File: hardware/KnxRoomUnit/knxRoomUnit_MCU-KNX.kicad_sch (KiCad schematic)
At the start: 26 parts, among them J1 KNX, J2 PROG, Q1 S8050, Q2 S8050, SW1 rst, SW2 UI_UP, SW3 KNX_PROG, SW4 UI_DW, SW5 UI_OK, U2 ESP32-WROOM-32

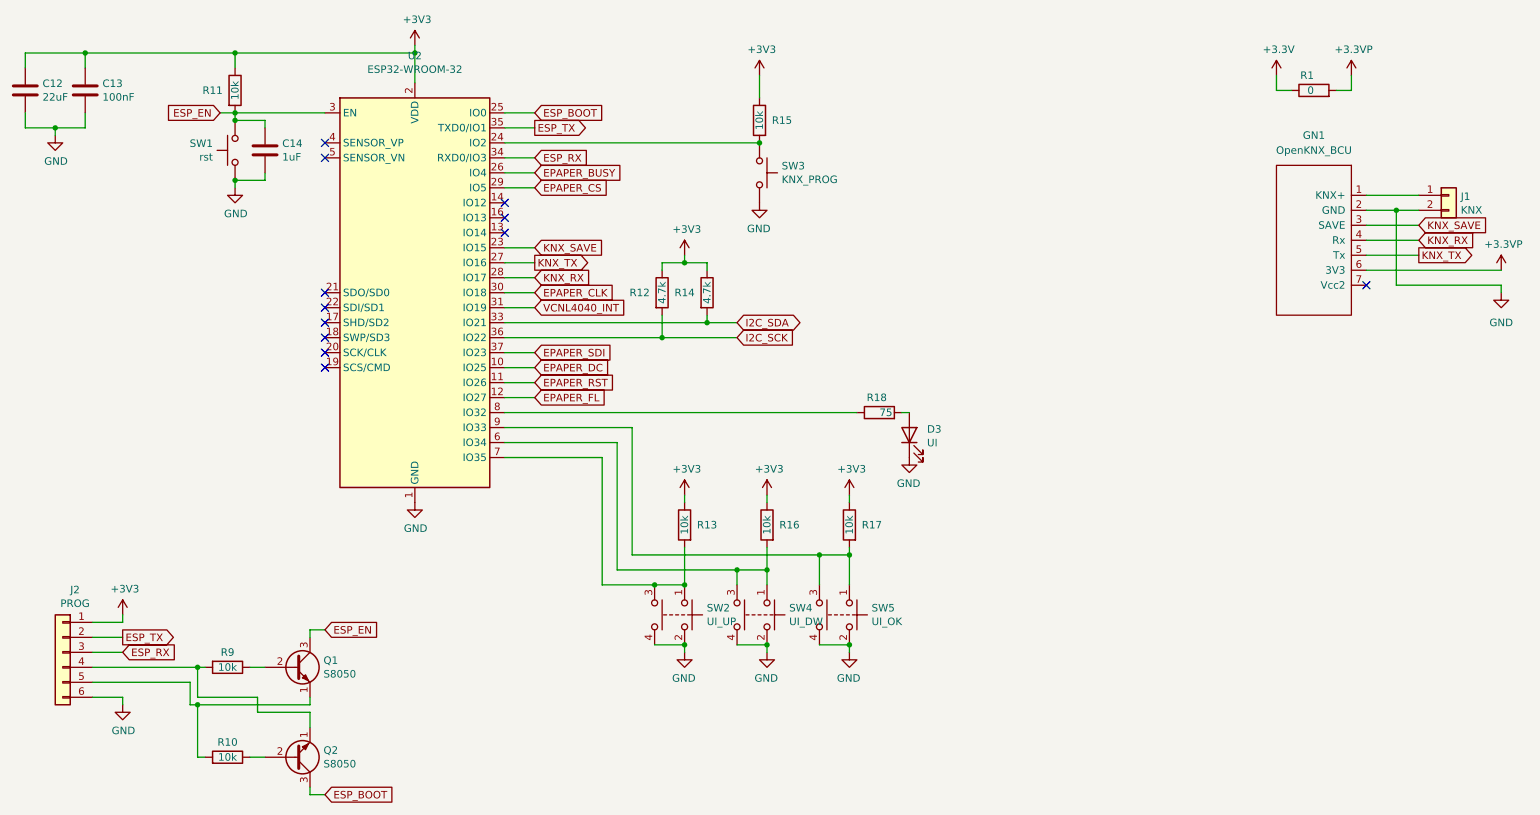
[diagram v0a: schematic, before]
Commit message: Updated sensors
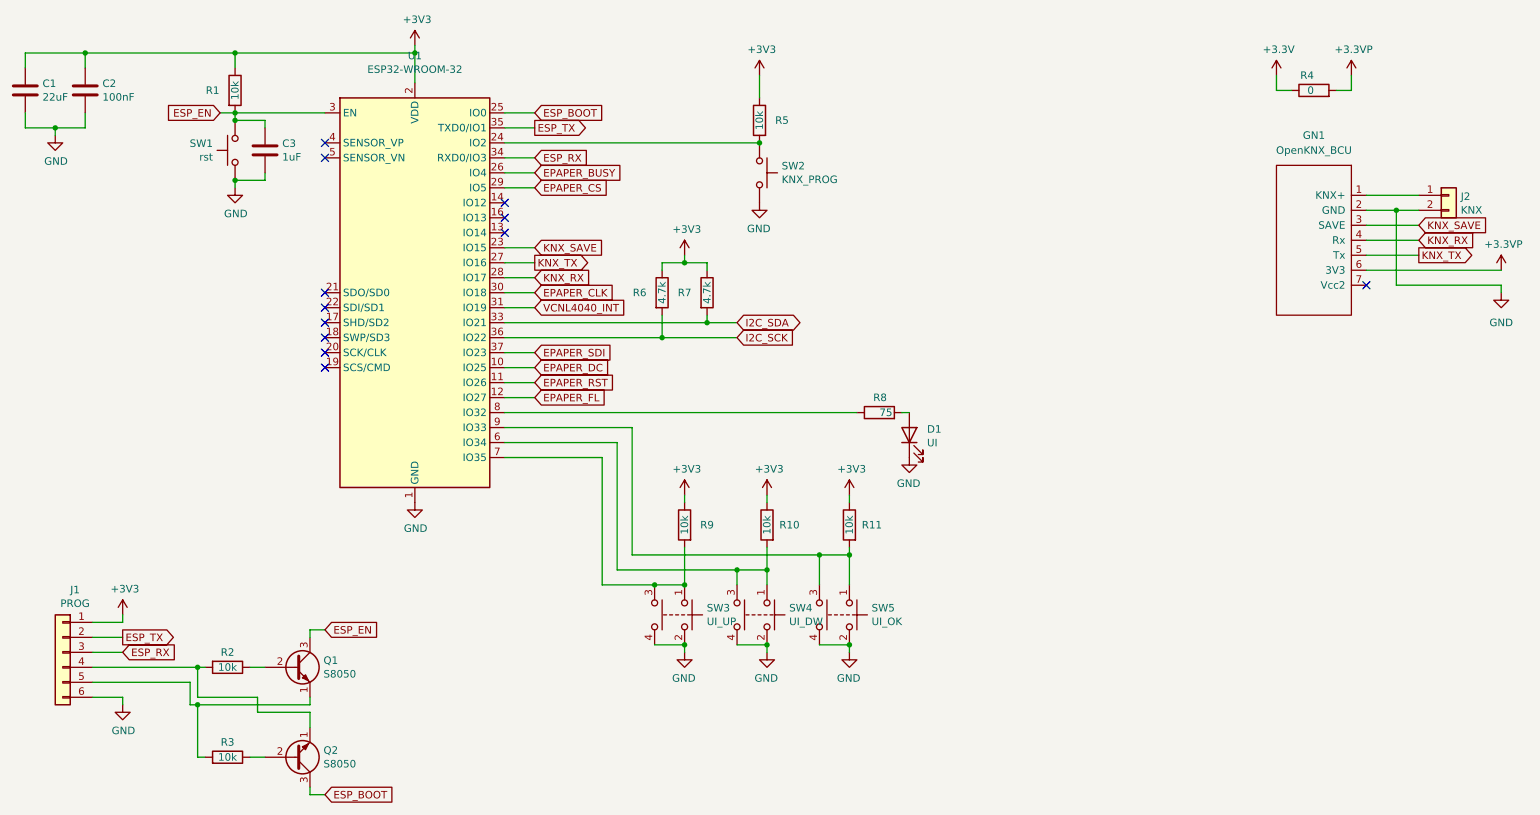
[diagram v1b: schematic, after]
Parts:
- renumbered C12 to C1, C13 to C2, C14 to C3, D3 to D1, J2 to J1, J1 to J2, R11 to R1, R16 to R10, R17 to R11, R9 to R2, R10 to R3, R1 to R4, R15 to R5, R12 to R6, R14 to R7, R18 to R8, R13 to R9, SW3 to SW2, SW2 to SW3, U2 to U1
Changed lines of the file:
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@@
   (symbol (lib_id "Switch:SW_Push_Dual") (at 130.81 118.11 270) (unit 1)
     (in_bom yes) (on_board yes) (dnp no)
-    (property "Reference" "SW2" (at 134.5692 116.9416 90)
+    (property "Reference" "SW3" (at 134.5692 116.9416 90)
       (effects (font (size 1.27 1.27)) (justify left))
     )
@@
       (project "knxRoomUnit"
         (path "/699feae1-8cdd-4d2b-947f-f24849c73cdb/00000000-0000-0000-0000-00006045b179"
-          (reference "SW2") (unit 1)
+          (reference "SW3") (unit 1)
         )
       )
@@
   (symbol (lib_id "Device:R") (at 130.81 102.87 0) (mirror y) (unit 1)
     (in_bom yes) (on_board yes) (dnp no)
-    (property "Reference" "R13" (at 134.62 102.87 0)
+    (property "Reference" "R9" (at 134.62 102.87 0)
       (effects (font (size 1.27 1.27)))
     )
@@
       (project "knxRoomUnit"
         (path "/699feae1-8cdd-4d2b-947f-f24849c73cdb/00000000-0000-0000-0000-00006045b179"
-          (reference "R13") (unit 1)
+          (reference "R9") (unit 1)
         )
       )
@@
   (symbol (lib_id "Device:R") (at 144.78 102.87 0) (mirror y) (unit 1)
     (in_bom yes) (on_board yes) (dnp no)
-    (property "Reference" "R16" (at 148.59 102.87 0)
+    (property "Reference" "R10" (at 148.59 102.87 0)
       (effects (font (size 1.27 1.27)))
     )
@@
       (project "knxRoomUnit"
         (path "/699feae1-8cdd-4d2b-947f-f24849c73cdb/00000000-0000-0000-0000-00006045b179"
-          (reference "R16") (unit 1)
+          (reference "R10") (unit 1)
         )
       )
@@
   (symbol (lib_id "Device:R") (at 158.75 102.87 0) (mirror y) (unit 1)
     (in_bom yes) (on_board yes) (dnp no)
-    (property "Reference" "R17" (at 162.56 102.87 0)
+    (property "Reference" "R11" (at 162.56 102.87 0)
       (effects (font (size 1.27 1.27)))
     )
@@
       (project "knxRoomUnit"
         (path "/699feae1-8cdd-4d2b-947f-f24849c73cdb/00000000-0000-0000-0000-00006045b179"
-          (reference "R17") (unit 1)
+          (reference "R11") (unit 1)
         )
       )
@@
   (symbol (lib_id "Device:C") (at 19.05 29.21 0) (unit 1)
     (in_bom yes) (on_board yes) (dnp no)
-    (property "Reference" "C12" (at 21.971 28.0416 0)
+    (property "Reference" "C1" (at 21.971 28.0416 0)
       (effects (font (size 1.27 1.27)) (justify left))
     )
@@
       (project "knxRoomUnit"
         (path "/699feae1-8cdd-4d2b-947f-f24849c73cdb/00000000-0000-0000-0000-00006045b179"
-          (reference "C12") (unit 1)
+          (reference "C1") (unit 1)
         )
       )
@@
   (symbol (lib_id "Device:C") (at 29.21 29.21 0) (unit 1)
     (in_bom yes) (on_board yes) (dnp no)
-    (property "Reference" "C13" (at 32.131 28.0416 0)
+    (property "Reference" "C2" (at 32.131 28.0416 0)
       (effects (font (size 1.27 1.27)) (justify left))
     )
@@
       (project "knxRoomUnit"
         (path "/699feae1-8cdd-4d2b-947f-f24849c73cdb/00000000-0000-0000-0000-00006045b179"
-          (reference "C13") (unit 1)
+          (reference "C2") (unit 1)
         )
       )
@@
   (symbol (lib_id "Device:R") (at 53.34 127 270) (unit 1)
     (in_bom yes) (on_board yes) (dnp no)
-    (property "Reference" "R9" (at 53.34 124.46 90)
+    (property "Reference" "R2" (at 53.34 124.46 90)
       (effects (font (size 1.27 1.27)))
     )
@@
       (project "knxRoomUnit"
         (path "/699feae1-8cdd-4d2b-947f-f24849c73cdb/00000000-0000-0000-0000-00006045b179"
-          (reference "R9") (unit 1)
+          (reference "R2") (unit 1)
         )
       )
@@
   (symbol (lib_id "Device:R") (at 53.34 142.24 270) (mirror x) (unit 1)
     (in_bom yes) (on_board yes) (dnp no)
-    (property "Reference" "R10" (at 53.34 139.7 90)
+    (property "Reference" "R3" (at 53.34 139.7 90)
       (effects (font (size 1.27 1.27)))
     )
@@
       (project "knxRoomUnit"
         (path "/699feae1-8cdd-4d2b-947f-f24849c73cdb/00000000-0000-0000-0000-00006045b179"
-          (reference "R10") (unit 1)
+          (reference "R3") (unit 1)
         )
       )
@@
   (symbol (lib_id "Connector_Generic:Conn_01x06") (at 25.4 124.46 0) (mirror y) (unit 1)
     (in_bom yes) (on_board yes) (dnp no)
-    (property "Reference" "J2" (at 27.4828 113.8682 0)
+    (property "Reference" "J1" (at 27.4828 113.8682 0)
       (effects (font (size 1.27 1.27)))
     )
@@
       (project "knxRoomUnit"
         (path "/699feae1-8cdd-4d2b-947f-f24849c73cdb/00000000-0000-0000-0000-00006045b179"
-          (reference "J2") (unit 1)
+          (reference "J1") (unit 1)
         )
       )
@@
   (symbol (lib_id "Switch:SW_Push") (at 143.51 43.18 270) (unit 1)
     (in_bom yes) (on_board yes) (dnp no)
-    (property "Reference" "SW3" (at 147.2692 42.0116 90)
+    (property "Reference" "SW2" (at 147.2692 42.0116 90)
       (effects (font (size 1.27 1.27)) (justify left))
     )
@@
       (project "knxRoomUnit"
         (path "/699feae1-8cdd-4d2b-947f-f24849c73cdb/00000000-0000-0000-0000-00006045b179"
-          (reference "SW3") (unit 1)
+          (reference "SW2") (unit 1)
         )
       )
@@
   (symbol (lib_id "Device:R") (at 143.51 34.29 0) (mirror y) (unit 1)
     (in_bom yes) (on_board yes) (dnp no)
-    (property "Reference" "R15" (at 147.32 34.29 0)
+    (property "Reference" "R5" (at 147.32 34.29 0)
       (effects (font (size 1.27 1.27)))
     )
@@
       (project "knxRoomUnit"
         (path "/699feae1-8cdd-4d2b-947f-f24849c73cdb/00000000-0000-0000-0000-00006045b179"
-          (reference "R15") (unit 1)
+          (reference "R5") (unit 1)
         )
       )
@@
   (symbol (lib_id "Device:R") (at 134.62 63.5 0) (unit 1)
     (in_bom yes) (on_board yes) (dnp no)
-    (property "Reference" "R14" (at 130.81 63.5 0)
+    (property "Reference" "R7" (at 130.81 63.5 0)
       (effects (font (size 1.27 1.27)))
     )
@@
       (project "knxRoomUnit"
         (path "/699feae1-8cdd-4d2b-947f-f24849c73cdb/00000000-0000-0000-0000-00006045b179"
-          (reference "R14") (unit 1)
+          (reference "R7") (unit 1)
         )
       )
@@
   (symbol (lib_id "Device:R") (at 127 63.5 0) (unit 1)
     (in_bom yes) (on_board yes) (dnp no)
-    (property "Reference" "R12" (at 123.19 63.5 0)
+    (property "Reference" "R6" (at 123.19 63.5 0)
       (effects (font (size 1.27 1.27)))
     )
@@
       (project "knxRoomUnit"
         (path "/699feae1-8cdd-4d2b-947f-f24849c73cdb/00000000-0000-0000-0000-00006045b179"
-          (reference "R12") (unit 1)
+          (reference "R6") (unit 1)
         )
       )
@@
   (symbol (lib_id "Device:R") (at 54.61 29.21 0) (unit 1)
     (in_bom yes) (on_board yes) (dnp no)
-    (property "Reference" "R11" (at 50.8 29.21 0)
+    (property "Reference" "R1" (at 50.8 29.21 0)
       (effects (font (size 1.27 1.27)))
     )
@@
       (project "knxRoomUnit"
         (path "/699feae1-8cdd-4d2b-947f-f24849c73cdb/00000000-0000-0000-0000-00006045b179"
-          (reference "R11") (unit 1)
+          (reference "R1") (unit 1)
         )
       )
@@
   (symbol (lib_id "RF_Module:ESP32-WROOM-32") (at 85.09 63.5 0) (unit 1)
     (in_bom yes) (on_board yes) (dnp no)
-    (property "Reference" "U2" (at 85.09 23.3426 0)
+    (property "Reference" "U1" (at 85.09 23.3426 0)
       (effects (font (size 1.27 1.27)))
     )
@@
       (project "knxRoomUnit"
         (path "/699feae1-8cdd-4d2b-947f-f24849c73cdb/00000000-0000-0000-0000-00006045b179"
-          (reference "U2") (unit 1)
+          (reference "U1") (unit 1)
         )
       )
@@
   (symbol (lib_id "Device:R") (at 163.83 83.82 90) (unit 1)
     (in_bom yes) (on_board yes) (dnp no)
-    (property "Reference" "R18" (at 165.1 81.28 90)
+    (property "Reference" "R8" (at 165.1 81.28 90)
       (effects (font (size 1.27 1.27)) (justify left))
     )
@@
       (project "knxRoomUnit"
         (path "/699feae1-8cdd-4d2b-947f-f24849c73cdb/00000000-0000-0000-0000-00006045b179"
-          (reference "R18") (unit 1)
+          (reference "R8") (unit 1)
         )
       )
@@
   (symbol (lib_id "Device:LED") (at 168.91 87.63 90) (unit 1)
     (in_bom yes) (on_board yes) (dnp no)
-    (property "Reference" "D3" (at 171.9072 86.6394 90)
+    (property "Reference" "D1" (at 171.9072 86.6394 90)
       (effects (font (size 1.27 1.27)) (justify right))
     )
@@
       (project "knxRoomUnit"
         (path "/699feae1-8cdd-4d2b-947f-f24849c73cdb/00000000-0000-0000-0000-00006045b179"
-          (reference "D3") (unit 1)
+          (reference "D1") (unit 1)
         )
       )
@@
   (symbol (lib_id "Device:C") (at 59.69 39.37 0) (unit 1)
     (in_bom yes) (on_board yes) (dnp no)
-    (property "Reference" "C14" (at 62.611 38.2016 0)
+    (property "Reference" "C3" (at 62.611 38.2016 0)
       (effects (font (size 1.27 1.27)) (justify left))
     )
@@
       (project "knxRoomUnit"
         (path "/699feae1-8cdd-4d2b-947f-f24849c73cdb/00000000-0000-0000-0000-00006045b179"
-          (reference "C14") (unit 1)
+          (reference "C3") (unit 1)
         )
       )
@@
   (symbol (lib_id "Device:R") (at 237.49 29.21 90) (unit 1)
     (in_bom yes) (on_board yes) (dnp no)
-    (property "Reference" "R1" (at 237.49 26.67 90)
+    (property "Reference" "R4" (at 237.49 26.67 90)
       (effects (font (size 1.27 1.27)) (justify left))
     )
@@
       (project "knxRoomUnit"
         (path "/699feae1-8cdd-4d2b-947f-f24849c73cdb/00000000-0000-0000-0000-00006045b179"
-          (reference "R1") (unit 1)
+          (reference "R4") (unit 1)
         )
       )
@@
   (symbol (lib_id "Connector_Generic:Conn_01x02") (at 260.35 46.99 0) (unit 1)
     (in_bom yes) (on_board yes) (dnp no)
-    (property "Reference" "J1" (at 262.382 47.1932 0)
+    (property "Reference" "J2" (at 262.382 47.1932 0)
       (effects (font (size 1.27 1.27)) (justify left))
     )
@@
       (project "knxRoomUnit"
         (path "/699feae1-8cdd-4d2b-947f-f24849c73cdb/00000000-0000-0000-0000-00006045b179"
-          (reference "J1") (unit 1)
-        )
-      )
+          (reference "J2") (unit 1)
+        )
+      )

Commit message: PCB routing
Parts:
- added D0: PWR, LED_SMD:LED_0603_1608Metric_Pad1.05x0.95mm_HandSolder, symbol Device:LED
- added R0: 75, Resistor_SMD:R_0603_1608Metric, symbol Device:R
- SW1: value rst -> RESET
- SW2: value KNX_PROG -> KNX
- SW3: value UI_UP -> DW
- SW4: value UI_DW -> OK
- SW5: value UI_OK -> UP
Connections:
- net +3V3: now also R0.1
- net GND: now also D0.1 (K)
- net SHT31_ALERT: now reaches U1.13 (IO14)
- new net: D0.2 (A), R0.2
- no-connect marks 12 -> 11
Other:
- moved on the sheet: GN1, J2

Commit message: Finished PCB routing
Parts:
- SW3, SW4, SW5: footprint (none) -> 431151008826:431151008826
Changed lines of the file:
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@@
       (effects (font (size 1.27 1.27)) (justify left))
     )
-    (property "Footprint" "" (at 135.89 118.11 0)
+    (property "Footprint" "431151008826:431151008826" (at 135.89 118.11 0)
       (effects (font (size 1.27 1.27)) hide)
     )
@@
       (effects (font (size 1.27 1.27)) (justify left))
     )
-    (property "Footprint" "" (at 149.86 118.11 0)
+    (property "Footprint" "431151008826:431151008826" (at 149.86 118.11 0)
       (effects (font (size 1.27 1.27)) hide)
     )
@@
       (effects (font (size 1.27 1.27)) (justify left))
     )
-    (property "Footprint" "" (at 163.83 118.11 0)
-      (effects (font (size 1.27 1.27)) hide)
-    )
+    (property "Footprint" "431151008826:431151008826" (at 163.83 118.11 0)
+      (effects (font (size 1.27 1.27)) hide)
+    )

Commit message: Production adjustments
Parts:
- D0, D1, GN1, J1, J2, SW1, SW2, SW3, SW4, SW5, U1: now left out of the parts list
- Q1, Q2: LCSC Part # C2146 -> C2150; Manufacturer Changjiang Electronics Tech (CJ) -> Jiangsu Changjing Electronics Technology Co., Ltd.; PartNumber S8050 -> SS8050
- R0, R8: LCSC Part # C25133 -> C21189; Manufacturer Uniroyal Elec -> UNI-ROYAL(Uniroyal Elec); PartNumber 0402WGF750JTCE -> 0603WAF0000T5E
- R1, R10, R11, R2, R3, R5, R9: LCSC Part # C25744 -> C25804; Manufacturer Uniroyal Elec -> UNI-ROYAL(Uniroyal Elec); PartNumber 0402WGF1002TCE -> 0603WAF1002T5E
- R4: Manufacturer Uniroyal Elec -> UNI-ROYAL(Uniroyal Elec)
- R6, R7: LCSC Part # C25900 -> C23162; Manufacturer Uniroyal Elec -> UNI-ROYAL(Uniroyal Elec); PartNumber 0402WGF4701TCE -> 0603WAF4701T5E
